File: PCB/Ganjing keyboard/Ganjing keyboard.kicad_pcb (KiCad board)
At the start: 2 copper layers, 304.8 x 122.8 mm, 176 parts, among them J1 Conn_01x04, J2 AVR-ISP-6, SW1 Rotary_Encoder_Switch, U1 ATmega32A-PU, Y1 Crystal

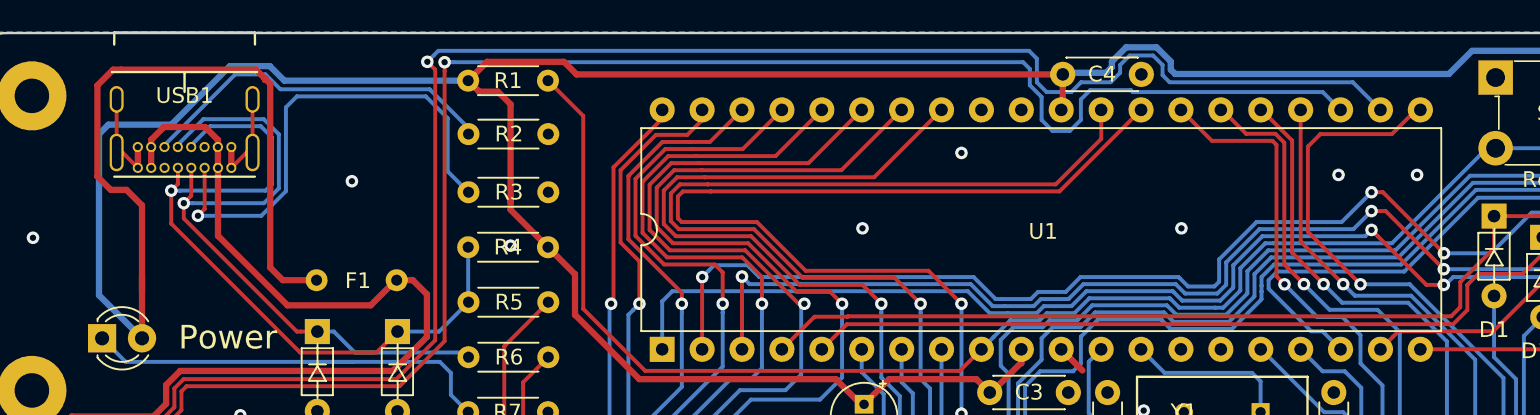
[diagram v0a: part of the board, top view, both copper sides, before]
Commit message: Adding a dope logo
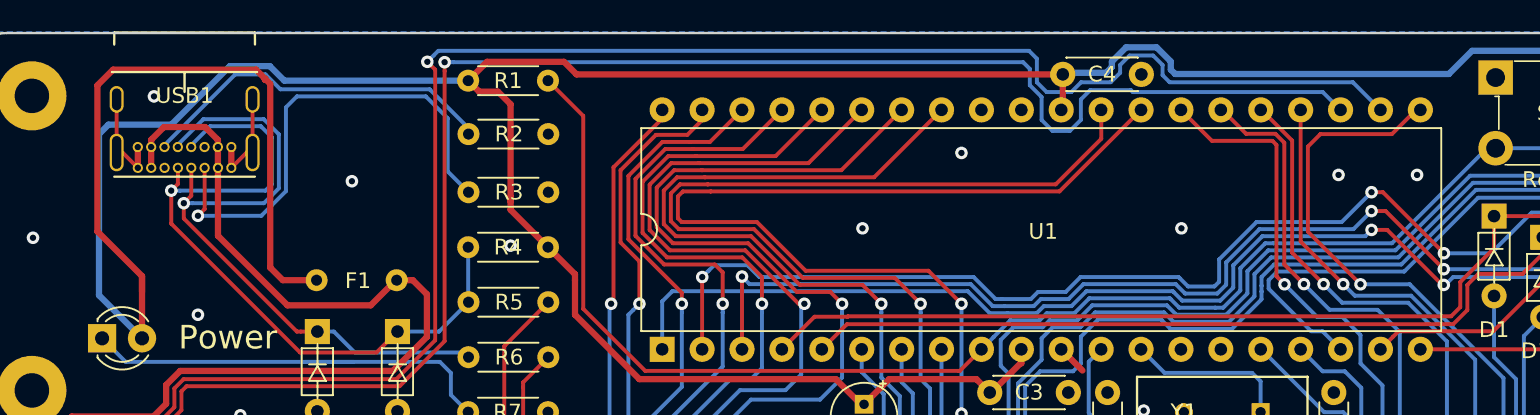
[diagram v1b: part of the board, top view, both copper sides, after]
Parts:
- added L1: LOGO, Logo:GanJing logo, F.Cu at (348.5, 102.2)
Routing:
- net +5V: track 242.6 -> 242.0 mm
- net GND: vias 138 -> 140

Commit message: Removing unnecessary drill holes
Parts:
- removed REF10, REF11, REF12, REF3, REF4, REF7, REF8, REF9: MountingHole_2.2mm_M2_Pad, Keyboard:MountingHole_2.2mm_M2_Pad
- MX31: value Caps Lock -> Standard
- MX59: value Ctrl -> 1.25u
- MX60: value Win -> 1.25u
- MX61: value Alt -> 1.25u
- MX62: value Space -> 6.25u
- MX69: value Stepped Caps Lock -> Stepped
- MX72: value 1.5u Ctrl -> 1.5u
- MX73: value 1.5u Alt -> 1.5u
- MX74: value 7.00u Space -> 7.00u
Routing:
- net Net-(D50-Pad2): track 124.9 -> 111.8 mm

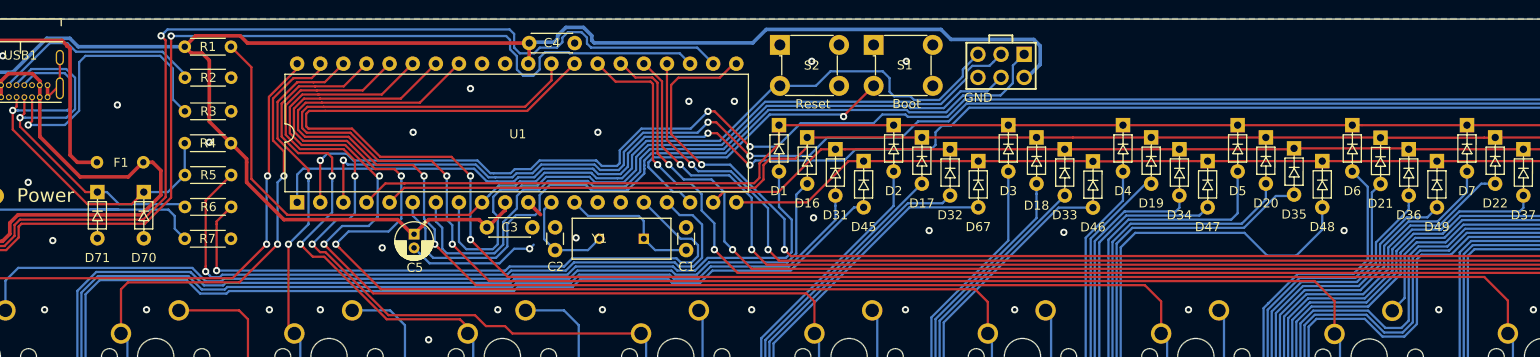
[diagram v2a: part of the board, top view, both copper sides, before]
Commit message: Cleaning up some routing
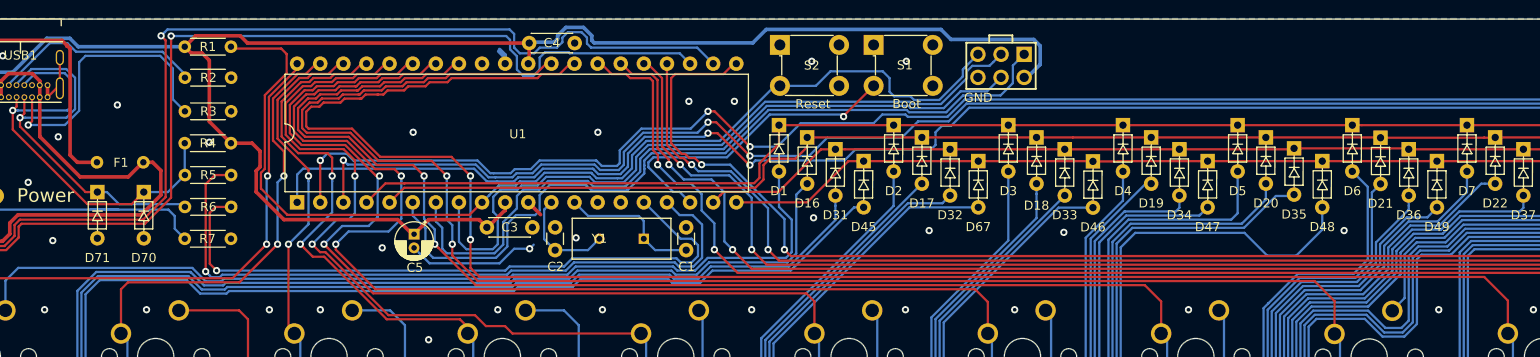
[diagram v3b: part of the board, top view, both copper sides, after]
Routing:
- net Reset: track 109.5 -> 115.0 mm
- net GND: track 29.5 -> 33.0 mm
- net col9: track 250.2 -> 252.2 mm
- net +5V: track 242.0 -> 243.7 mm
- net D+: track 70.7 -> 72.3 mm
- net D-: track 76.3 -> 77.4 mm
- net SW15A: track 325.3 -> 326.4 mm

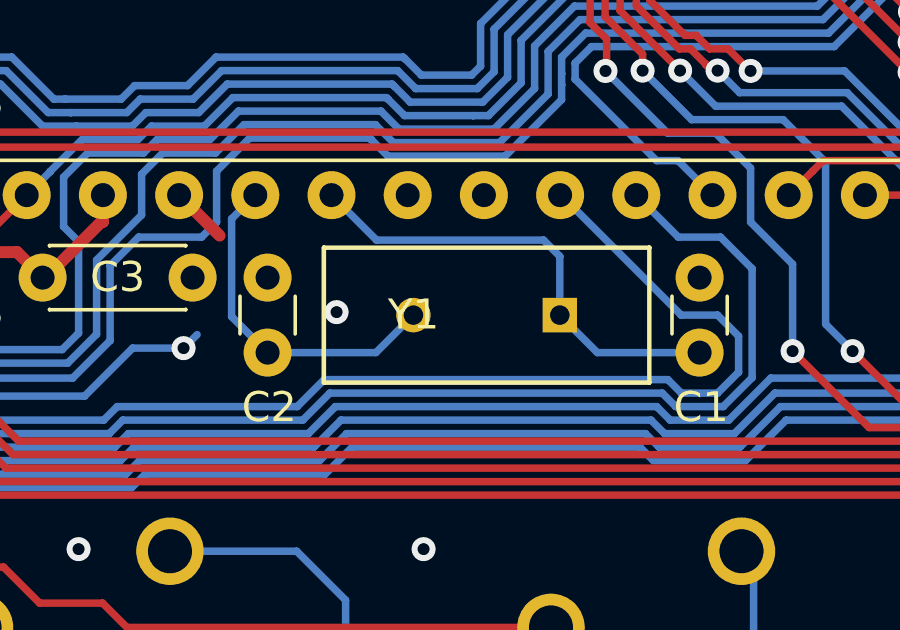
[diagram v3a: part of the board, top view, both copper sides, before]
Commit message: Altering case to centre screw holes and adjust angle of stand to exactly 6 degrees
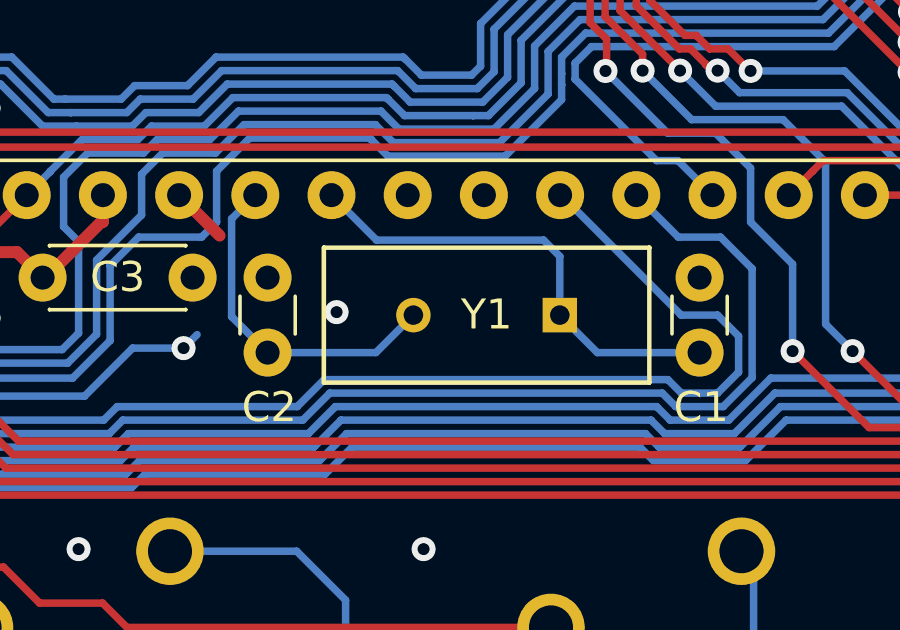
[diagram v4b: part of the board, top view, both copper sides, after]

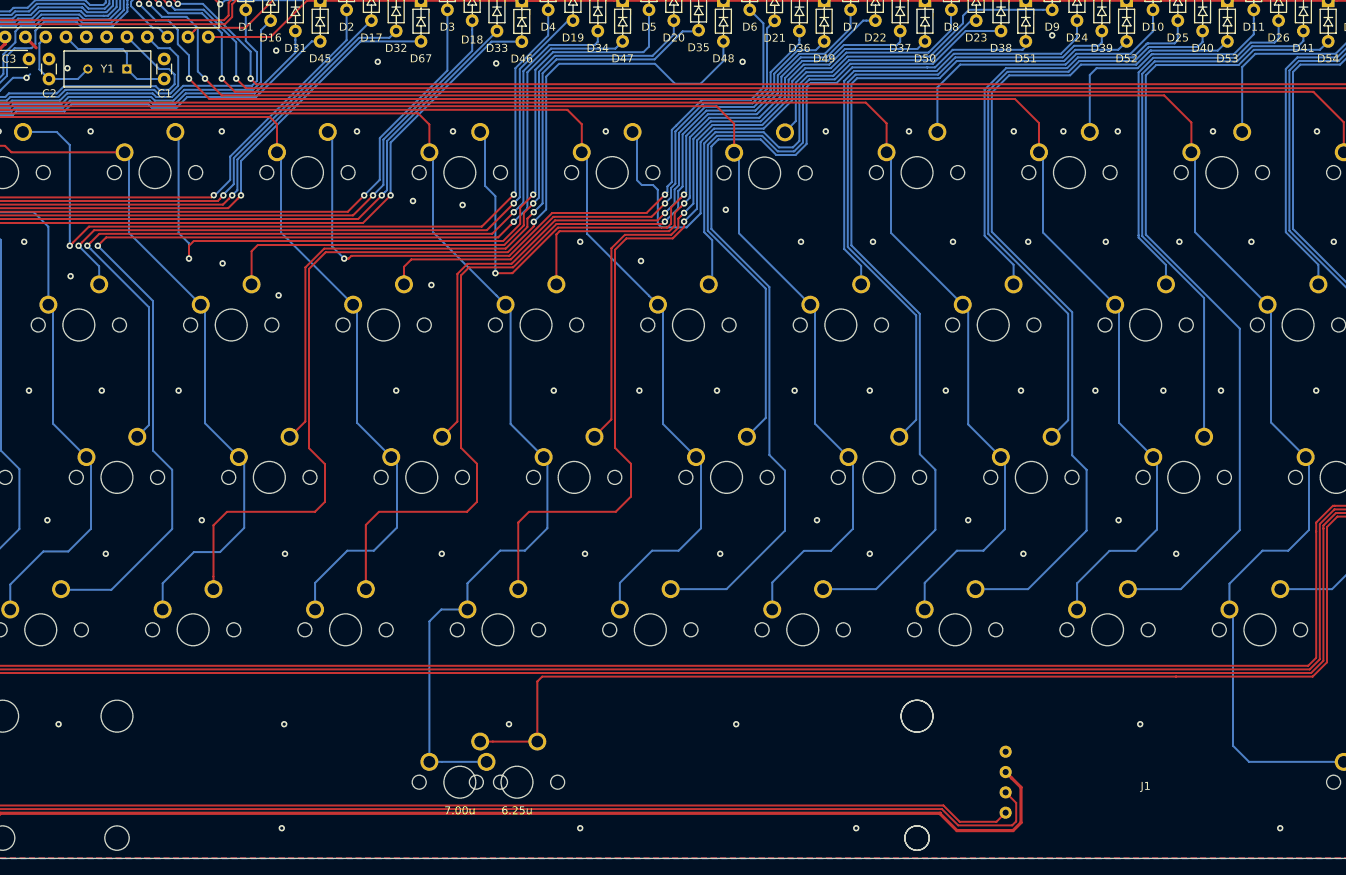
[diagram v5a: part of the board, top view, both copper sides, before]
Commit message: Adding 3d models
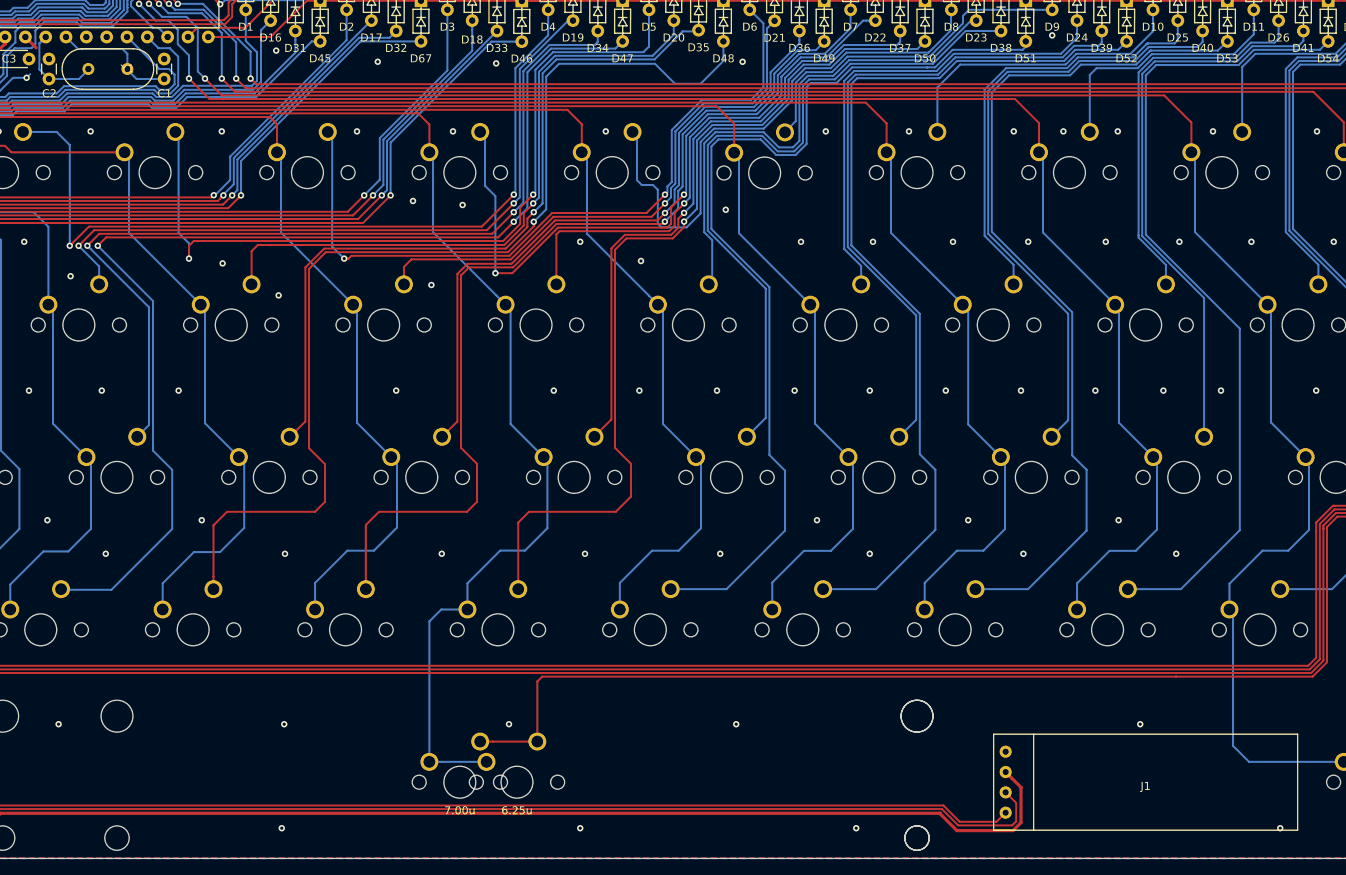
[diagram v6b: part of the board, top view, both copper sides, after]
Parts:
- J1: footprint Keyboard:ssd1306 128x32 oled -> Keyboard:ssd1306_128x32_oled
- USB1: value USB_C_GCT_USB4085 -> USB_C_USB4085
- Y1: footprint GanJing-crystal:CTS-ATS16B-0 -> Keyboard:Crystal_HC49-4H_Vertical
- moved Y1 2.50 mm to (141.8, 120.4)
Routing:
- net GND: vias 140 -> 139

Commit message: Fixing crystal footprint
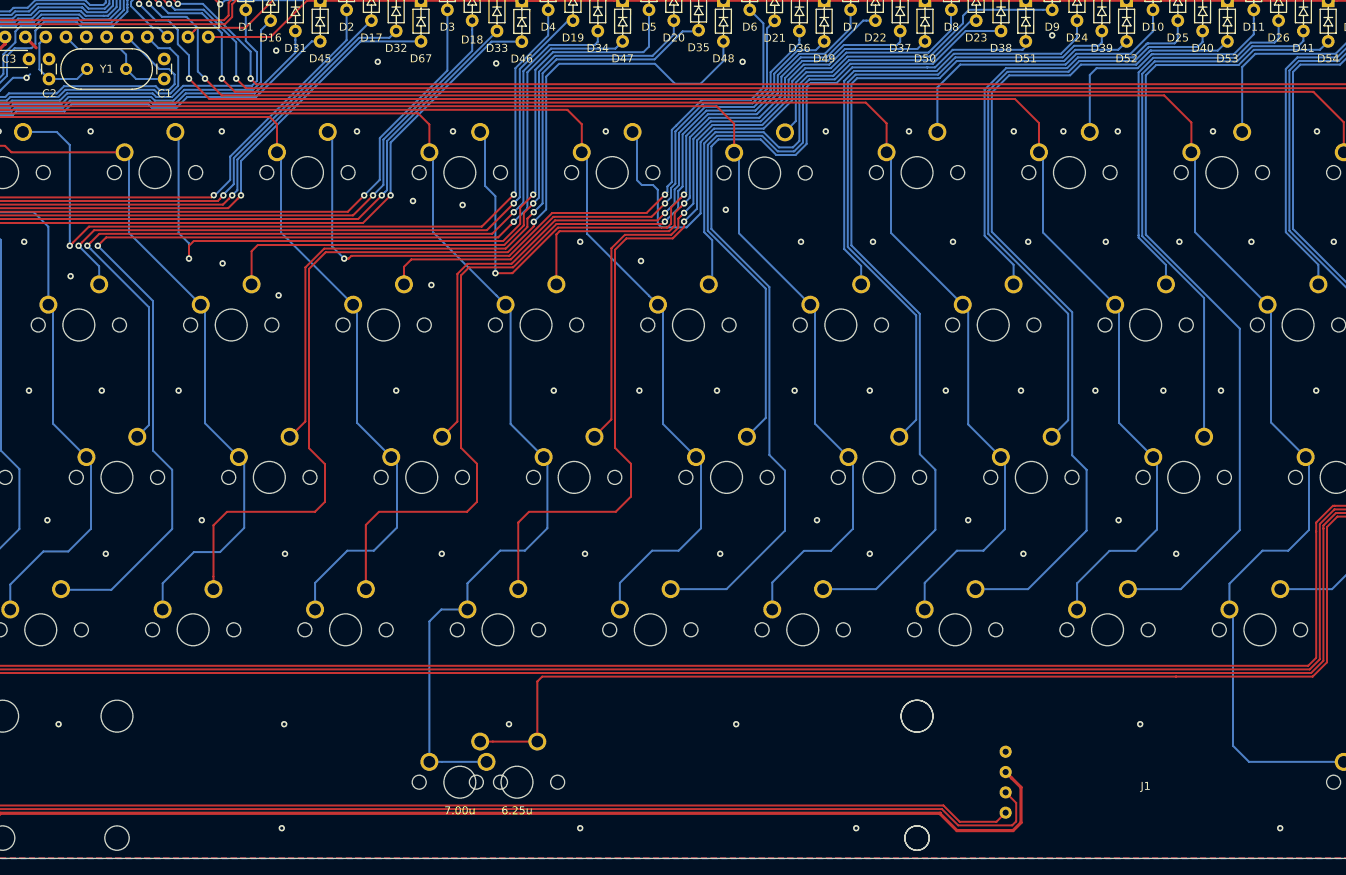
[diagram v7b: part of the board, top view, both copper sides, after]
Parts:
- moved Y1 0.16 mm to (141.6, 120.4)

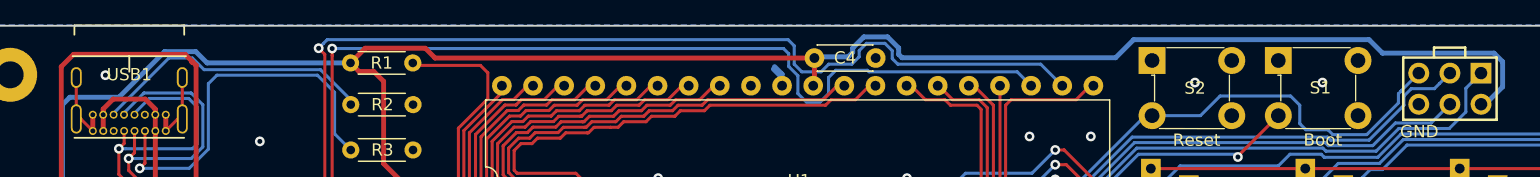
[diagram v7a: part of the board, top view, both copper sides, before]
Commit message: Cleaning up silk screen
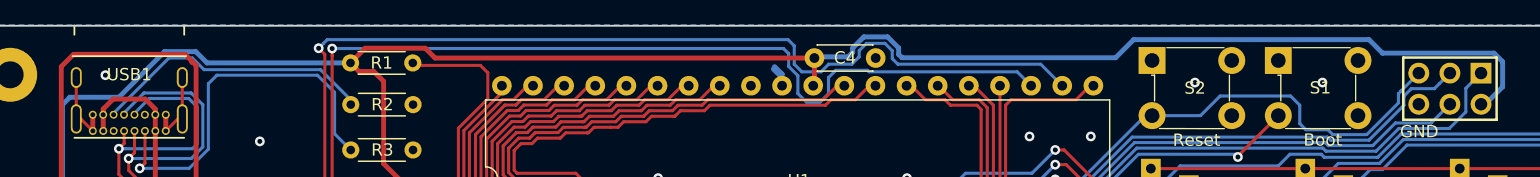
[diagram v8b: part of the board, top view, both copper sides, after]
